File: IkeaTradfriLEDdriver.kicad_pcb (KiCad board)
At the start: 2 copper layers, 16 parts, among them J1 input, J2 IKEA Zigbit module, J3 led strip, Q1 BUZ11, Q2 BC547, U1 LM741, U2 LM1117-3.3

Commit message: Naroutovana deska
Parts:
- J1: footprint Connector_Wire:SolderWirePad_1x02_P5.08mm_Drill1.5mm -> Connector_PinHeader_2.54mm:PinHeader_1x02_P2.54mm_Horizontal
- U1: footprint Package_DIP:DIP-8_W10.16mm_LongPads -> Package_DIP:DIP-8_W7.62mm_LongPads
- moved R4 48.2 mm to (162.6, 101.0), turned to 180 degrees
- moved R3 46.9 mm to (155.6, 72.4), turned to 180 degrees
- moved J3 43.4 mm to (173.4, 83.8)
- moved J1 40.0 mm to (106.7, 80.0), turned to 180 degrees
- moved U1 32.3 mm to (144.8, 85.7), turned to 90 degrees
- moved C1 32.2 mm to (120.7, 94.0)
- moved D1 25.9 mm to (139.7, 80.0), turned to 180 degrees
- moved R1 25.5 mm to (139.7, 85.1), turned to 180 degrees
- moved C2 21.5 mm to (116.2, 91.4), turned to 180 degrees
- moved Q1 18.4 mm to (160.0, 78.1), turned to 270 degrees
- moved C3 17.6 mm to (121.3, 99.7), turned to 270 degrees
- moved U2 14.5 mm to (116.2, 102.2), turned to 90 degrees
- moved C4 14.0 mm to (129.5, 101.6), turned to 90 degrees
- moved Q2 13.4 mm to (161.3, 91.4)
- moved R2 9.47 mm to (139.7, 91.4)
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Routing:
- net +12V: track 0.00 -> 84.8 mm
- net +3V3: track 0.00 -> 32.2 mm
- net Net-(J3-Pad1): track 0.00 -> 20.4 mm
- net Net-(D1-Pad1): track 0.00 -> 16.8 mm
- net Net-(Q2-Pad1): track 0.00 -> 16.7 mm
- net Net-(R3-Pad2): track 0.00 -> 9.59 mm
- net Net-(Q2-Pad2): track 0.00 -> 9.53 mm
- net Net-(Q1-Pad1): track 0.00 -> 7.56 mm
- net pwm: track 0.00 -> 5.08 mm
- net (no net): vias 0 -> 4
- added copper zone on B.Cu, net GND
- added copper zone on F.Cu, net GND
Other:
- board outline added: 89.5 x 44.4 mm

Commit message: Deska naroutovana jako jednovrstva, vsechny cesty na spodku
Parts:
- Q2: footprint Package_TO_SOT_THT:TO-92_Inline -> Package_TO_SOT_THT:TO-92L_HandSolder
- moved Q2 0.63 mm to (160.7, 91.4), turned to 270 degrees
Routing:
- net Net-(Q2-Pad2): track 9.53 -> 13.8 mm
- net Net-(R3-Pad2): track 9.59 -> 12.4 mm
- net +12V: track 84.8 -> 84.2 mm
- net Net-(Q2-Pad1): track 16.7 -> 16.1 mm
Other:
- board text added: "Heatsink"

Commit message: Provedene opravy na desce
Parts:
- removed J1: input, Connector_PinHeader_2.54mm:PinHeader_1x02_P2.54mm_Horizontal
- added H1: +, MountingHole:MountingHole_2.5mm_Pad, F.Cu at (108.6, 76.2)
- added H2: -, MountingHole:MountingHole_2.5mm_Pad, F.Cu at (108.6, 83.2)
- Q1, U2: footprint Package_TO_SOT_THT:TO-220-3_Vertical -> Package_TO_SOT_THT:TO-220-3_Horizontal_TabDown
- moved R1 17.6 mm to (128.3, 71.8), turned to 270 degrees
- moved D1 17.1 mm to (123.2, 84.5), turned to 90 degrees
- moved C2 15.1 mm to (130.2, 97.2), turned to 270 degrees
- moved U1 13.9 mm to (141.7, 72.1), turned to 270 degrees
- moved R4 12.5 mm to (159.4, 88.9), turned to 0 degrees
- moved R2 10.8 mm to (131.4, 84.5)
- moved C4 10.8 mm to (137.2, 94.0)
- moved U2 8.26 mm to (123.8, 99.1)
- moved C1 8.03 mm to (128.3, 91.4)
- moved J3 7.62 mm to (173.4, 91.4)
- moved Q2 7.41 mm to (154.3, 87.6)
- moved R3 7.28 mm to (148.3, 71.6), turned to 270 degrees
- moved Q1 6.84 mm to (153.7, 75.6)
- moved C3 5.80 mm to (127.1, 99.7)
- moved J2 3.24 mm to (148.0, 104.1)
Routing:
- net +12V: track 84.2 -> 58.5 mm
- net Net-(Q2-Pad1): track 16.1 -> 35.1 mm
- net pwm: track 5.08 -> 23.4 mm
- net Net-(Q2-Pad2): track 13.8 -> 3.81 mm
- net Net-(D1-Pad1): track 16.8 -> 25.5 mm
- net Net-(R3-Pad2): track 12.4 -> 19.2 mm
- net Net-(J3-Pad1): track 20.4 -> 25.9 mm
- net +3V3: track 32.2 -> 33.1 mm
- removed copper zone on F.Cu, net GND
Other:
- board size 89.5 x 44.4 mm -> 89.5 x 39.4 mm
- board text added: "Protahnout draty"
- board text added: "Zigbee module naplocho"
- board text removed: "Heatsink"

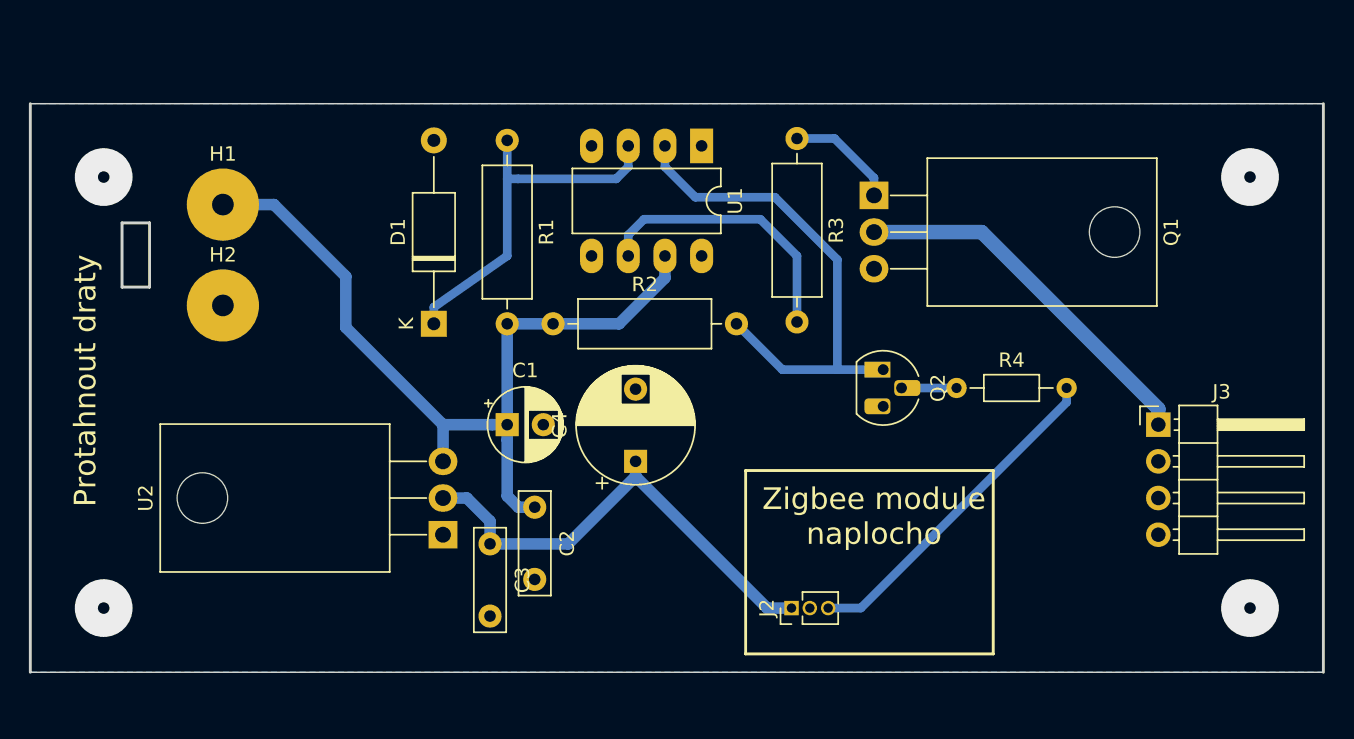
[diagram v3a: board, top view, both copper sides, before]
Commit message: Nejake divoke a nepovedene upravy
Stahoval jsem aktualizaci 3d modelu, ale do slozky se neda zapsat, takze 6 hodin cekani a smula :(
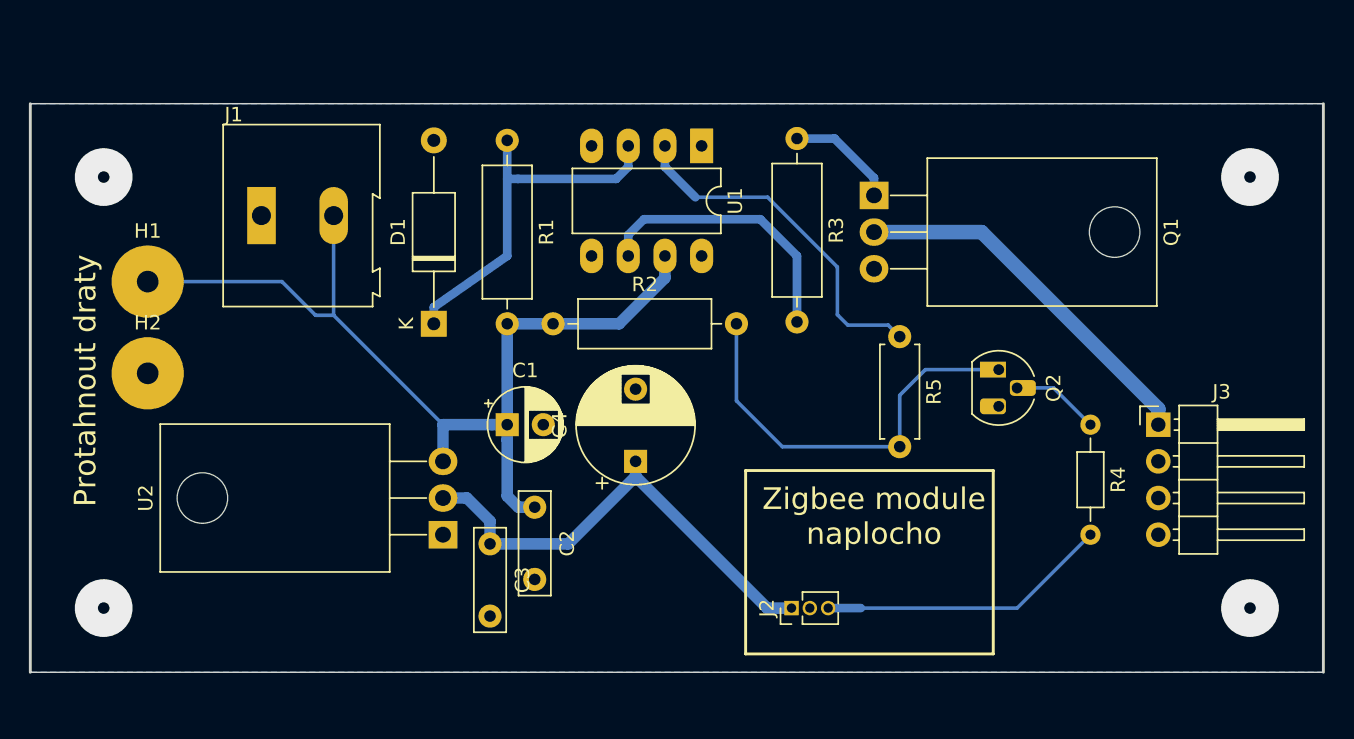
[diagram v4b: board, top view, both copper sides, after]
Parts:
- added J1: zdroj, TerminalBlock:TerminalBlock_Altech_AK300-2_P5.00mm, F.Cu at (111.3, 77.0)
- added R5: 10k, Resistor_THT:R_Axial_DIN0207_L6.3mm_D2.5mm_P7.62mm_Horizontal, F.Cu at (155.4, 85.3)
- moved R4 9.61 mm to (168.7, 91.4), turned to 270 degrees
- moved Q2 8.00 mm to (162.3, 87.6)
- moved H1 7.45 mm to (103.4, 81.5)
- moved H2 7.01 mm to (103.4, 87.9)
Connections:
- U1 pad 2: Net-(Q2-Pad1) -> Net-(R5-Pad1)
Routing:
- net Net-(R5-Pad1): track 0.00 -> 24.5 mm
- net +12V: track 58.5 -> 66.4 mm
- net Net-(Q2-Pad1): track 35.1 -> 29.1 mm
- net pwm: track 23.4 -> 20.3 mm
- net Net-(Q2-Pad2): track 3.81 -> 6.13 mm
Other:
- outline, holes or cut-outs redrawn
